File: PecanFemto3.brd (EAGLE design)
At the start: 28.9 x 10.2 mm, 37 parts, among them IC1 SPV1040T, IC3 EVA7M, IC4 SI4060/3, IC5 LPC824M201JHI33E, U1 TPS62203DBVT

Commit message: Routed parts
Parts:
- moved ANTENNA 15.7 mm to (11.3, 16.5), flipped to the bottom
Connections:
- net CS_RADIO: now also IC5.10; no longer IC5.9
- net IRQ: now also IC5.14; no longer IC5.13
- net MISO: now also IC5.12; no longer IC5.11
- net MOSI: now also IC5.11; no longer IC5.10
- net RADIO_SDN: now also IC5.9
- net SCK: now also IC5.13; no longer IC5.12
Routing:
- net RADIO_SDN: track 0.00 -> 7.32 mm, vias 0 -> 2
- net VCC: track 51.1 -> 55.0 mm
- net GND: vias 34 -> 35

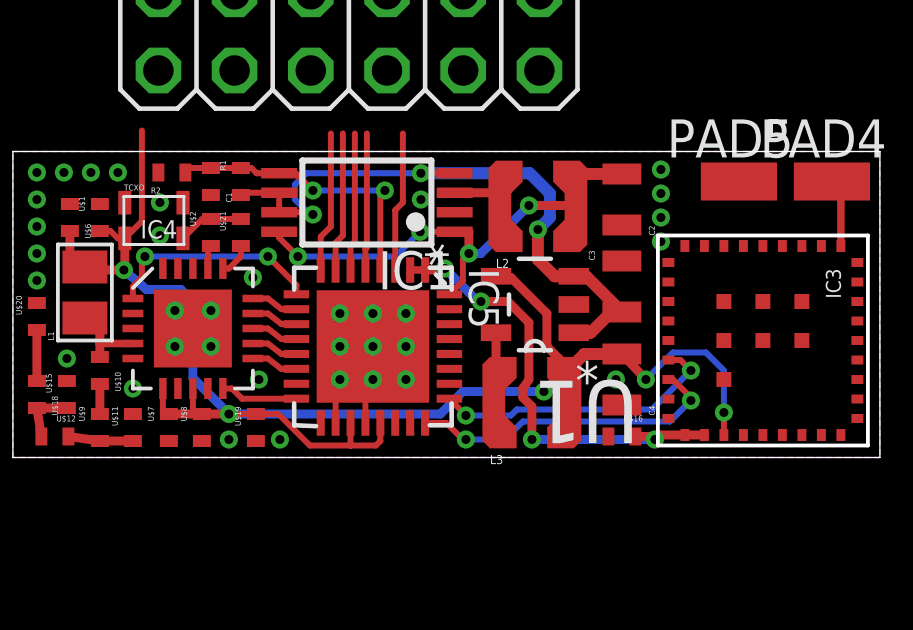
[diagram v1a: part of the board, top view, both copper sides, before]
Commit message: Connected GND
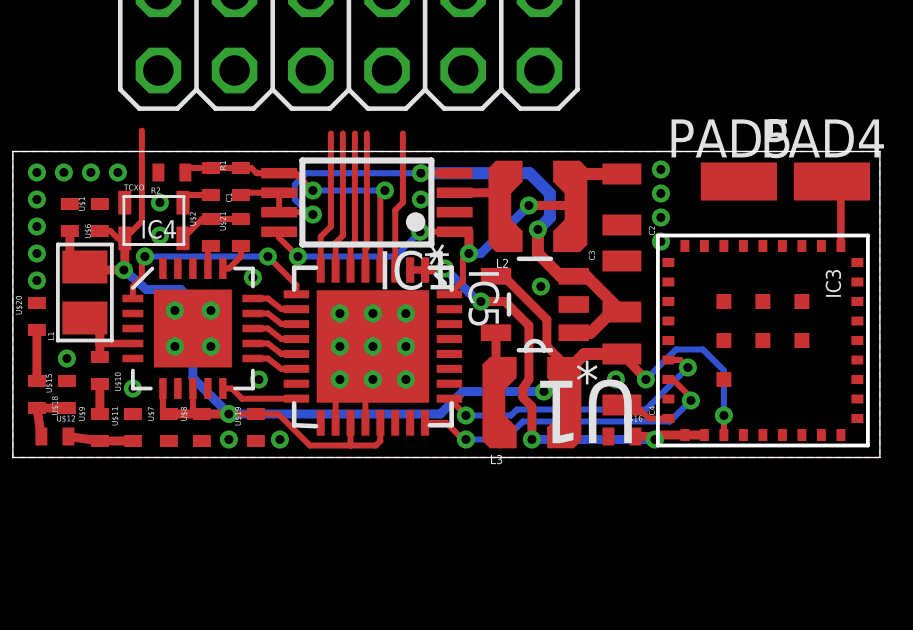
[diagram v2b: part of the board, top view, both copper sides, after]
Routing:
- net GND: track 4.74 -> 7.66 mm, vias 35 -> 36
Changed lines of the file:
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@@
 <wire x1="18.5" y1="18.8" x2="17.4" y2="18.8" width="0.25" layer="1"/>
 </signal>
-<signal name="GND" airwireshidden="yes">
+<signal name="GND">
 <contactref element="U$6" pad="P$2"/>
 <contactref element="U$11" pad="P$1"/>
@@
 <via x="19.4" y="23.5" extent="1-16" drill="0.3"/>
 <via x="19.4" y="22.4" extent="1-16" drill="0.3"/>
+<wire x1="34.8" y1="16.75" x2="35.25" y2="16.75" width="0.2" layer="1"/>
+<wire x1="35.25" y1="16.75" x2="35.7" y2="16.3" width="0.2" layer="1"/>
+<wire x1="35.7" y1="16.3" x2="36.35" y2="16.3" width="0.2" layer="1"/>
+<via x="32.1" y="20.7" extent="1-16" drill="0.3"/>
 <wire x1="32.05" y1="27.9" x2="32.05" y2="30.44" width="0" layer="19" extent="1-1"/>
 <wire x1="29.51" y1="30.44" x2="32.05" y2="30.44" width="0" layer="19" extent="1-1"/>
 <wire x1="36.1" y1="24.6" x2="32.05" y2="27.9" width="0" layer="19" extent="1-1"/>
 <wire x1="36.1" y1="22.2" x2="36.1" y2="23" width="0" layer="19" extent="1-1"/>
-<wire x1="21.1" y1="23.75" x2="20.17" y2="23.495" width="0" layer="19" extent="1-1"/>
-<wire x1="36.35" y1="16.3" x2="34.8" y2="16.75" width="0" layer="19" extent="1-1"/>
-<wire x1="33.1954" y1="20.1" x2="34.8" y2="21.55" width="0" layer="19" extent="1-1"/>
-<wire x1="38.2" y1="17.6" x2="36.35" y2="16.3" width="0" layer="19" extent="1-1"/>
 <wire x1="21.89" y1="27.9" x2="19.35" y2="24.5" width="0" layer="19" extent="1-1"/>
 <wire x1="1" y1="8.4" x2="16.3" y2="17.55" width="0" layer="19" extent="1-1"/>
 <wire x1="-5.4" y1="8.4" x2="1" y2="8.4" width="0" layer="19" extent="1-1"/>
+<wire x1="20.17" y1="23.495" x2="20.17" y2="23.75" width="0.2" layer="1"/>
+<wire x1="20.17" y1="23.75" x2="21.1" y2="23.75" width="0.2" layer="1"/>
 </signal>
 <signal name="N$4">
@@
 <wire x1="34.8" y1="18.45" x2="35.6" y2="17.6" width="0.3" layer="1"/>
 <via x="35.6" y="17.6" extent="1-16" drill="0.3"/>
-<via x="38.2" y="16.5" extent="1-16" drill="0.3"/>
-<wire x1="38.2" y1="16.5" x2="38.2" y2="15.75" width="0.2" layer="1"/>
+<via x="38.2" y="16.4" extent="1-16" drill="0.3"/>
+<wire x1="38.2" y1="16.4" x2="38.2" y2="15.75" width="0.2" layer="1"/>
 <wire x1="33.1977625" y1="18.1007625" x2="32.7525" y2="18.227" width="0.2" layer="1"/>
 <wire x1="32.7525" y1="18.227" x2="32.4985" y2="17.87775" width="0.2" layer="1"/>
@@
 <wire x1="32.4985" y1="15.78225" x2="32.7525" y2="15.433" width="0.2" layer="1"/>
 <wire x1="32.7525" y1="15.433" x2="33.1977625" y2="15.5592375" width="0.2" layer="1"/>
-<wire x1="38.2" y1="17.9" x2="38.2" y2="16.5" width="0.2" layer="16"/>
+<wire x1="38.2" y1="17.9" x2="38.2" y2="16.4" width="0.2" layer="16"/>
 <contactref element="U$1" pad="P$2"/>
 <contactref element="TCXO" pad="4"/>
@@
 <wire x1="26.7485" y1="15.5485" x2="26.7485" y2="16.15" width="0.2" layer="1"/>
 <via x="32.2" y="17.2" extent="1-16" drill="0.3"/>
-<wire x1="35.6" y1="17.6" x2="36.5" y2="18.5" width="0.2" layer="16"/>
-<wire x1="36.5" y1="18.5" x2="37.6" y2="18.5" width="0.2" layer="16"/>
-<wire x1="37.6" y1="18.5" x2="38.2" y2="17.9" width="0.2" layer="16"/>
+<wire x1="35.6" y1="17.6" x2="36.6" y2="18.6" width="0.2" layer="16"/>
+<wire x1="36.6" y1="18.6" x2="37.5" y2="18.6" width="0.2" layer="16"/>
+<wire x1="37.5" y1="18.6" x2="38.2" y2="17.9" width="0.2" layer="16"/>
 <wire x1="34.8" y1="18.45" x2="33.547" y2="18.45" width="0.4" layer="1"/>
 <wire x1="33.547" y1="18.45" x2="33.1977625" y2="18.1007625" width="0.4" layer="1"/>
 <wire x1="32.4985" y1="17.87775" x2="32.6985" y2="18.3015" width="0.3" layer="1"/>
 <wire x1="32.6985" y1="18.3015" x2="32.3" y2="18.7" width="0.3" layer="1"/>
-<wire x1="32.3" y1="18.7" x2="32.3" y2="19.8" width="0.3" layer="1"/>
+<wire x1="32.3" y1="18.7" x2="32.3" y2="19.6" width="0.3" layer="1"/>
 <wire x1="22.6" y1="16.45" x2="21.7" y2="16.45" width="0.2" layer="1"/>
 <wire x1="26.6" y1="15.4" x2="25.7545" y2="15.4" width="0.2" layer="1"/>
@@
 <wire x1="32.2" y1="17.2" x2="32.652959375" y2="17.652959375" width="0.3" layer="1"/>
 <wire x1="32.652959375" y1="17.652959375" x2="32.689" y2="17.652959375" width="0.3" layer="1"/>
-<wire x1="30.6046" y1="20.9954" x2="31.1046" y2="20.9954" width="0.3" layer="1"/>
-<wire x1="31.1046" y1="20.9954" x2="32.3" y2="19.8" width="0.3" layer="1"/>
+<wire x1="30.6046" y1="20.9954" x2="30.9046" y2="20.9954" width="0.3" layer="1"/>
+<wire x1="30.9046" y1="20.9954" x2="32.3" y2="19.6" width="0.3" layer="1"/>
 <wire x1="18.23" y1="22.305" x2="18.8" y2="22.875" width="0.2" layer="1"/>
 <wire x1="18.8" y1="22.875" x2="18.8" y2="25.9" width="0.2" layer="1"/>
@@
 <wire x1="33.1954" y1="21.0398" x2="33.6102" y2="21.0398" width="0.4" layer="1"/>
 <wire x1="33.6102" y1="21.0398" x2="34.8" y2="19.85" width="0.4" layer="1"/>
-<wire x1="32" y1="22.6" x2="32" y2="21.6" width="0.4" layer="1"/>
-<wire x1="32" y1="21.6" x2="32.5602" y2="21.0398" width="0.4" layer="1"/>
-<wire x1="32.5602" y1="21.0398" x2="33.1954" y2="21.0398" width="0.4" layer="1"/>
+<wire x1="32" y1="22.6" x2="32" y2="21.8" width="0.4" layer="1"/>
+<wire x1="32" y1="21.8" x2="32.7602" y2="21.0398" width="0.4" layer="1"/>
+<wire x1="32.7602" y1="21.0398" x2="33.1954" y2="21.0398" width="0.4" layer="1"/>
 <via x="24.5" y="23.1" extent="1-16" drill="0.3"/>
 <wire x1="24.5" y1="23.1" x2="24.4" y2="23.1" width="0.2" layer="16"/>
@@
 <contactref element="ANTENNA" pad="1"/>
 <wire x1="15.3" y1="19.25" x2="15.3" y2="17.55" width="0.3" layer="1"/>
-<wire x1="11.3" y1="16.5" x2="15.3" y2="17.55" width="0" layer="19" extent="1-1"/>
+<wire x1="11.3" y1="16.5" x2="15.3" y2="17.55" width="0" layer="19" extent="1-16"/>
 </signal>
 <signal name="OUT2">
@@
 <via x="30.1" y="20.2" extent="1-16" drill="0.3"/>
 <wire x1="30.1" y1="20.2" x2="30" y2="20.2" width="0.3" layer="16"/>
-<wire x1="30.1" y1="20.2" x2="31" y2="20.2" width="0.3" layer="1"/>
-<wire x1="31" y1="20.2" x2="31.7" y2="19.5" width="0.3" layer="1"/>
+<wire x1="30.1" y1="20.2" x2="30.9" y2="20.2" width="0.3" layer="1"/>
+<wire x1="30.9" y1="20.2" x2="31.7" y2="19.4" width="0.3" layer="1"/>
 <wire x1="31.7" y1="15.7" x2="31.8" y2="15.6" width="0.3" layer="1"/>
 <wire x1="30" y1="20.2" x2="28.9" y2="21.3" width="0.3" layer="16"/>
-<wire x1="31.7" y1="19.5" x2="31.7" y2="17.6" width="0.3" layer="1"/>
+<wire x1="31.7" y1="19.4" x2="31.7" y2="17.6" width="0.3" layer="1"/>
 <wire x1="31.7" y1="17.6" x2="31.5" y2="17.3" width="0.3" layer="1"/>
 <wire x1="31.5" y1="17.3" x2="31.5" y2="17" width="0.3" layer="1"/>
@@
 <signal name="RXD">
 <contactref element="IC3" pad="P$15"/>
-<via x="37.1" y="17.9" extent="1-16" drill="0.3"/>
-<wire x1="37.1" y1="17.9" x2="36.75" y2="18.25" width="0.2" layer="1"/>
+<via x="37" y="18" extent="1-16" drill="0.3"/>
+<wire x1="37" y1="18" x2="36.75" y2="18.25" width="0.2" layer="1"/>
 <wire x1="36.75" y1="18.25" x2="36.35" y2="18.25" width="0.2" layer="1"/>
 <wire x1="29.6" y1="16.4" x2="31.1" y2="16.4" width="0.2" layer="16"/>
 <wire x1="31.1" y1="16.4" x2="31.3" y2="16.6" width="0.2" layer="16"/>
-<wire x1="31.3" y1="16.6" x2="35.8" y2="16.6" width="0.2" layer="16"/>
+<wire x1="31.3" y1="16.6" x2="35.6" y2="16.6" width="0.2" layer="16"/>
 <via x="29.6" y="16.4" extent="1-16" drill="0.3"/>
-<wire x1="35.8" y1="16.6" x2="37.1" y2="17.9" width="0.2" layer="16"/>
+<wire x1="35.6" y1="16.6" x2="37" y2="18" width="0.2" layer="16"/>
 <contactref element="IC5" pad="25"/>
 <wire x1="29.05" y1="16.96" x2="29.61" y2="16.4" width="0.2" layer="1"/>

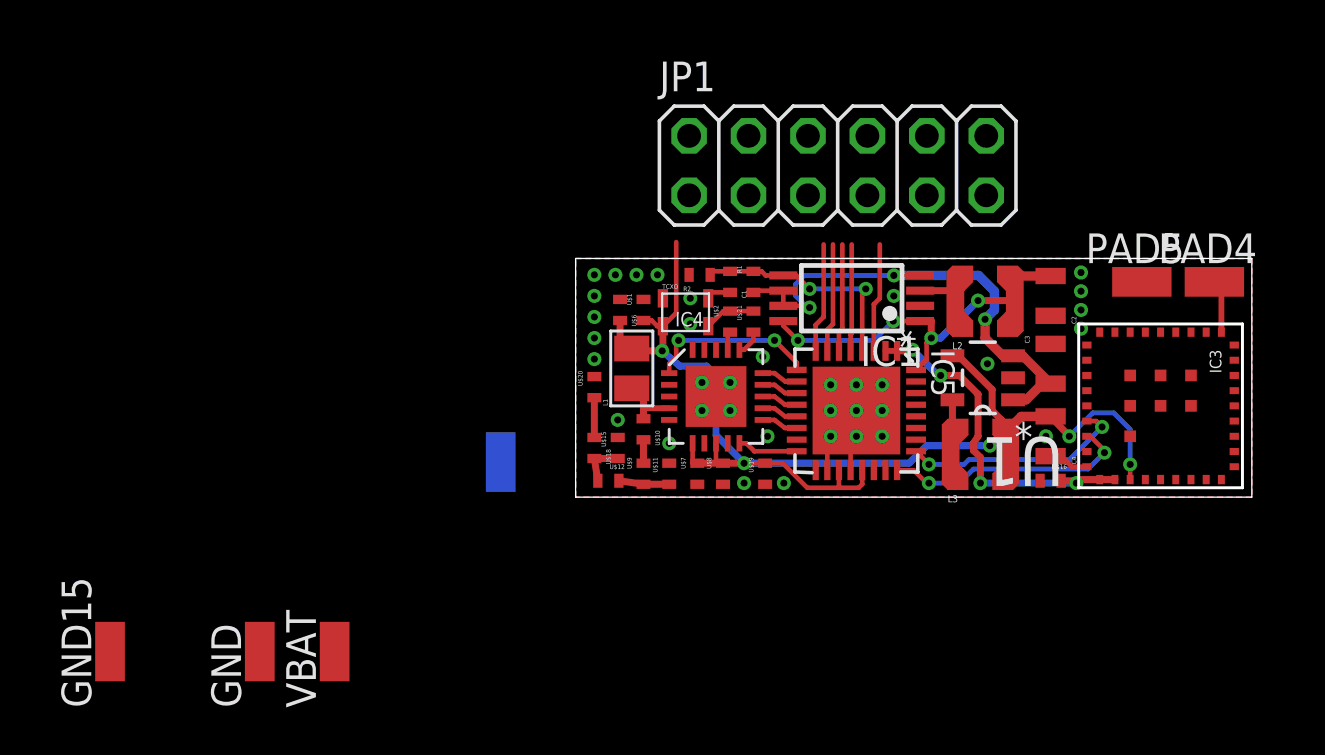
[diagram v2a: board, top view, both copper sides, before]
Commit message: Moved parts, updated libs, added pads, added programmer pins
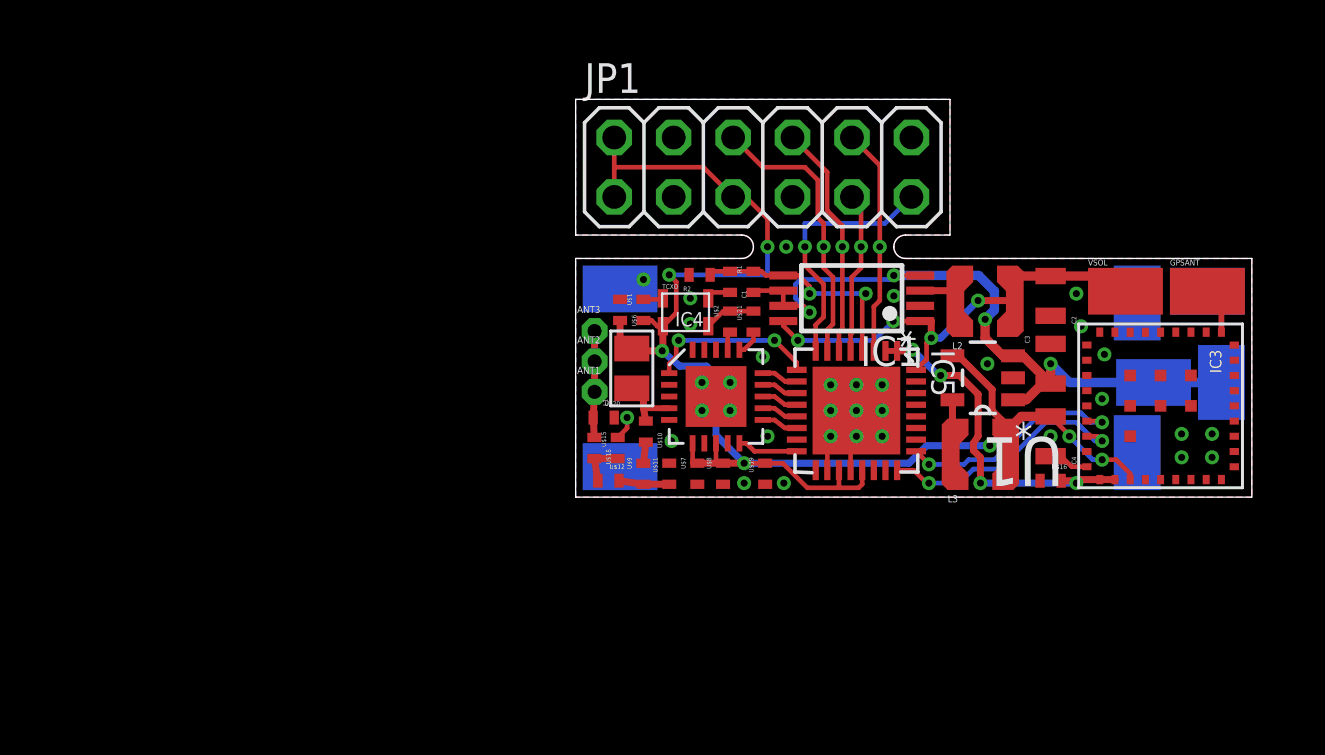
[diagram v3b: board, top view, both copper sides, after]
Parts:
- removed ANTENNA, GND, PAD4, PAD5: (no value), PecanFemto4:SMD1,27-2,54
- added ANT1, ANT2, ANT3: TP, testpad:P1-7
- added GND24, GND28, GND29, GND30, GPSANT, VBAT1, VSOL: (no value), PecanFemto4:SMD1,27-2,54
- moved VBAT 39.6 mm to (42.1, 19.9), flipped to the bottom
- moved GND15 26.7 mm to (16.4, 23.9), flipped to the bottom, turned to 270 degrees
- moved JP1 3.20 mm to (22.5, 29.1)
- moved U$20 1.36 mm to (15.7, 18.4), turned to 180 degrees
- moved U$10 0.14 mm to (17.5, 17.8)
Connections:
- removed net OUT3: JP1.4
- removed net OUT4: JP1.2
- net GND: now also GND24.1, GND28.1, GND29.1, GND30.1, JP1.4, JP1.7; no longer GND.1, JP1.10, JP1.11, PAD5.1
- net N$1: now also GPSANT.1; no longer PAD4.1
- net N$3: now also ANT1.TP, ANT2.TP, ANT3.TP; no longer ANTENNA.1
- net OUT1: now also JP1.9; no longer JP1.8
- net OUT2: now also JP1.11; no longer JP1.6
- net RESET: now also JP1.10; no longer JP1.9
- net SWCLK: now also JP1.8; no longer JP1.7
- net SWDIO: now also JP1.6; no longer JP1.5
- net VBAT: now also VBAT1.1
- net VCC: now also JP1.2, JP1.5
- net VSOLAR: now also VSOL.1
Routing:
- net VCC: track 55.0 -> 68.4 mm, vias 5 -> 7
- net VBAT: track 22.2 -> 30.9 mm, vias 3 -> 4
- net SWDIO: track 4.65 -> 12.0 mm, vias 0 -> 1
- net OUT2: track 4.69 -> 10.9 mm, vias 0 -> 1
- net SWCLK: track 4.61 -> 10.1 mm, vias 0 -> 1
- net RESET: track 4.66 -> 9.72 mm, vias 0 -> 1
- net VSOLAR: track 19.6 -> 23.6 mm
- net N$3: track 1.70 -> 4.55 mm
- net OUT1: track 4.57 -> 6.93 mm, vias 0 -> 1
- net GND: track 7.66 -> 9.55 mm, vias 36 -> 34
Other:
- board size 28.9 x 10.2 mm -> 28.9 x 17 mm

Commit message: Added via
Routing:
- net GND: vias 34 -> 35
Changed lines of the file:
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@@
 <via x="37" y="19.2" extent="1-16" drill="0.3"/>
 <via x="37.1" y="21.1" extent="1-16" drill="0.3"/>
+<via x="31.6" y="21.2" extent="1-16" drill="0.3"/>
 </signal>
 <signal name="N$4">
